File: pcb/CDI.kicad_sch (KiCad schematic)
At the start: 32 parts, among them K501 Relay, Q501 MMBT2222A, Q502 MMBTA55, Q503 MMBT2222A, Q504 MMBTA55, Q505 MMBT2222A

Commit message: revision 2.0: changed R and C footprints to 0805 (imperial)
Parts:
- R501, R502, R503, R504, R505, R506, R507, R508, R509, R510: footprint Resistor_SMD:R_0603_1608Metric -> Resistor_SMD:R_0805_2012Metric
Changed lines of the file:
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@@
 			)
 		)
-		(property "Footprint" "Resistor_SMD:R_0603_1608Metric"
+		(property "Footprint" "Resistor_SMD:R_0805_2012Metric"
 			(at 116.84 65.278 90)
 			(effects
@@
 			)
 		)
-		(property "Footprint" "Resistor_SMD:R_0603_1608Metric"
+		(property "Footprint" "Resistor_SMD:R_0805_2012Metric"
 			(at 192.532 147.32 90)
 			(effects
@@
 			)
 		)
-		(property "Footprint" "Resistor_SMD:R_0603_1608Metric"
+		(property "Footprint" "Resistor_SMD:R_0805_2012Metric"
 			(at 234.188 58.42 90)
 			(effects
@@
 			)
 		)
-		(property "Footprint" "Resistor_SMD:R_0603_1608Metric"
+		(property "Footprint" "Resistor_SMD:R_0805_2012Metric"
 			(at 65.532 116.84 90)
 			(effects
@@
 			)
 		)
-		(property "Footprint" "Resistor_SMD:R_0603_1608Metric"
+		(property "Footprint" "Resistor_SMD:R_0805_2012Metric"
 			(at 54.102 137.16 90)
 			(effects
@@
 			)
 		)
-		(property "Footprint" "Resistor_SMD:R_0603_1608Metric"
+		(property "Footprint" "Resistor_SMD:R_0805_2012Metric"
 			(at 185.42 144.018 90)
 			(effects
@@
 			)
 		)
-		(property "Footprint" "Resistor_SMD:R_0603_1608Metric"
+		(property "Footprint" "Resistor_SMD:R_0805_2012Metric"
 			(at 184.15 64.008 90)
 			(effects
@@
 			)
 		)
-		(property "Footprint" "Resistor_SMD:R_0603_1608Metric"
+		(property "Footprint" "Resistor_SMD:R_0805_2012Metric"
 			(at 48.26 133.858 90)
 			(effects
@@
 			)
 		)
-		(property "Footprint" "Resistor_SMD:R_0603_1608Metric"
+		(property "Footprint" "Resistor_SMD:R_0805_2012Metric"
 			(at 95.25 138.938 90)
 			(effects
@@
 			)
 		)
-		(property "Footprint" "Resistor_SMD:R_0603_1608Metric"
+		(property "Footprint" "Resistor_SMD:R_0805_2012Metric"
 			(at 144.272 48.26 90)
 			(effects

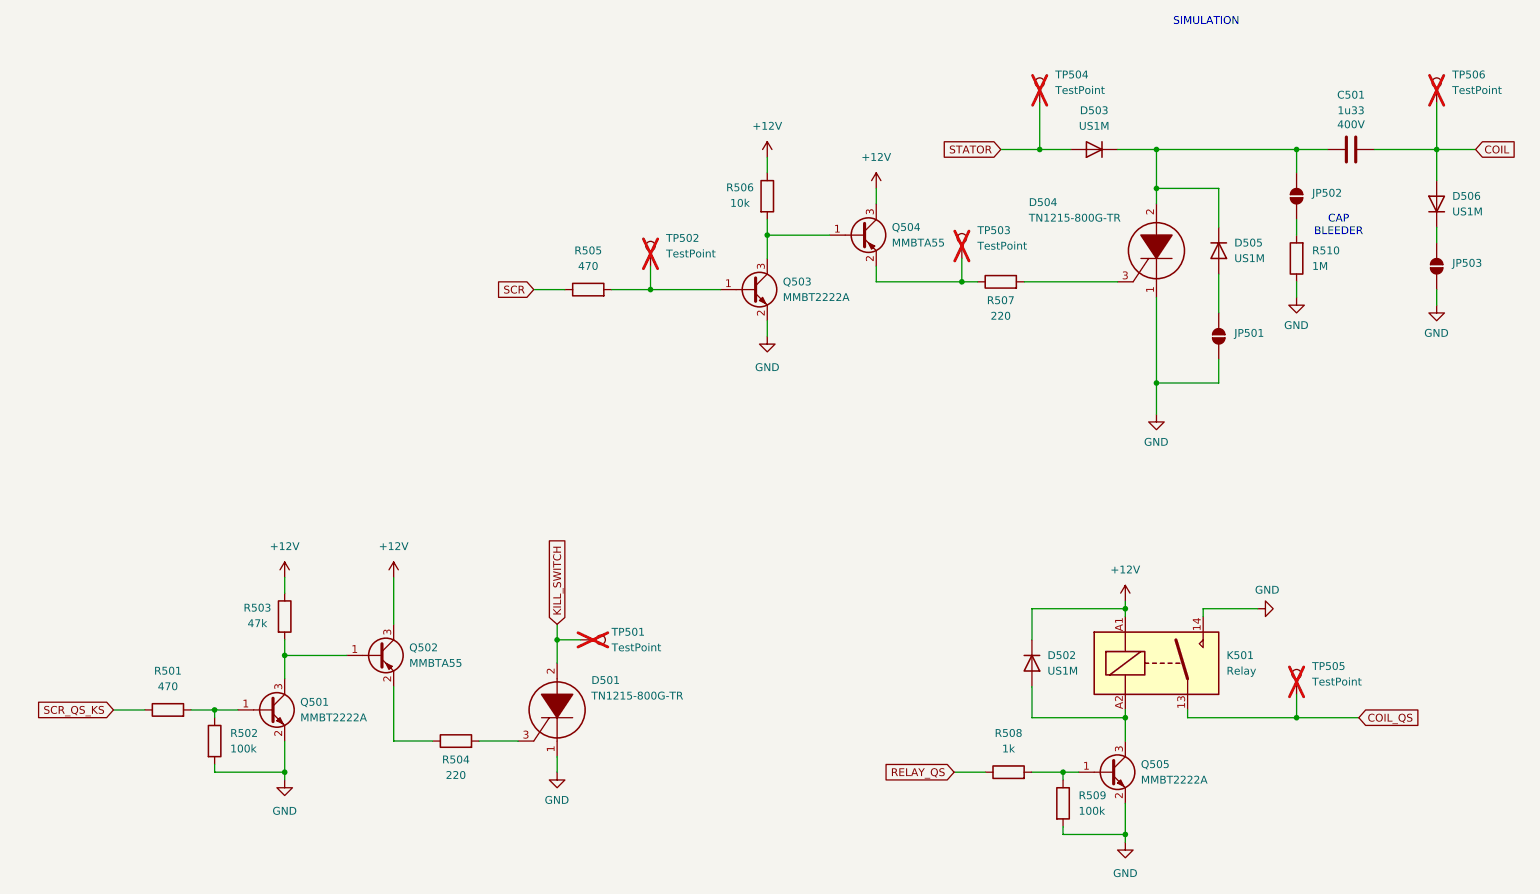
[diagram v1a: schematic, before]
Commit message: added testing comments
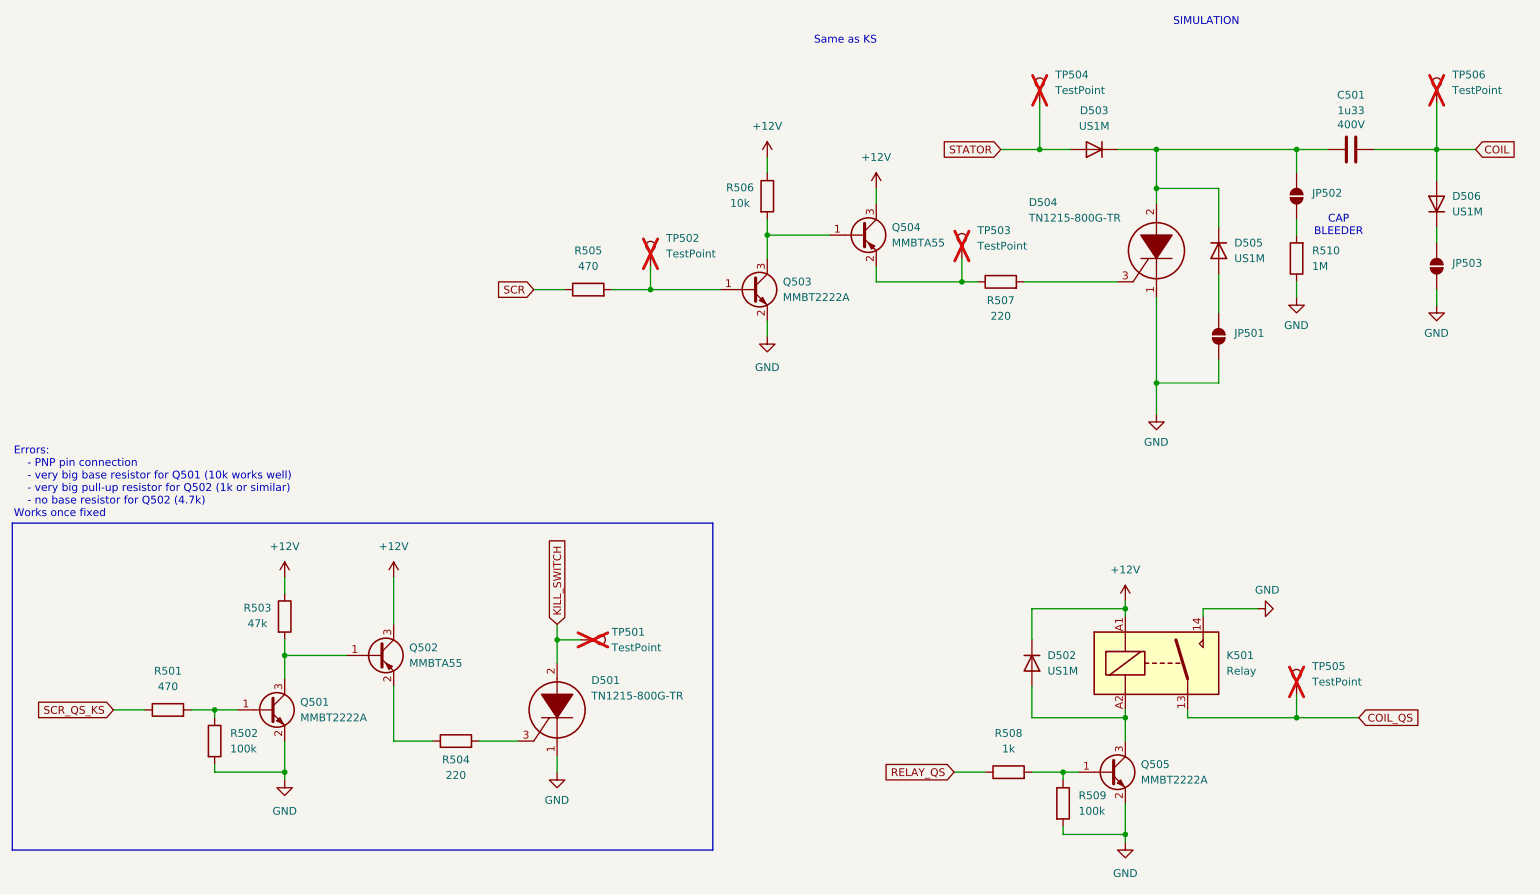
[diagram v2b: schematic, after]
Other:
- note added: "Errors: - PNP pin connection - very big base resistor for Q501 (10k works well) - very big pull-up resistor for Q502 (1k or similar) - no base resistor for Q502 (4.7k) Works once fixed"
- note added: "Same as KS"
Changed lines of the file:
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@@
 	(generator_version "9.0")
 	(paper "A4")
+	(rectangle
+		(start 22.86 101.6)
+		(end 137.16 154.94)
+		(stroke
+			(width 0)
+			(type solid)
+			(color 255 114 254 1)
+		)
+		(fill
+			(type none)
+		)
+	)
+	(text "Same as KS"
+		(exclude_from_sim no)
+		(at 153.67 22.86 0)
+		(effects
+			(font
+				(size 1.27 1.27)
+				(color 255 114 254 1)
+			)
+			(justify left)
+		)
+	)
 	(text "SIMULATION"
 		(exclude_from_sim no)
@@
 		)
 	)
+	(text "Errors:\n	- PNP pin connection\n	- very big base resistor for Q501 (10k works well)\n	- very big pull-up resistor for Q502 (1k or similar)\n	- no base resistor for Q502 (4.7k)\nWorks once fixed"
+		(exclude_from_sim no)
+		(at 23.114 94.996 0)
+		(effects
+			(font
+				(size 1.27 1.27)
+				(color 255 114 254 1)
+			)
+			(justify left)
+		)
+	)
